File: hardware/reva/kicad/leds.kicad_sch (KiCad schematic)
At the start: 38 parts

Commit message: feat(reva): 15 LED nets on the 595 chain, four more spare outputs
Spec 2026-10-07 section 5: 15 lamps (LED0..LED14), 73 pots. U_SR4 keeps
LED11..LED14 and gains SR_SPARE8..11, marked no-connect (four more test
points would wrap the chains sheet past the A3 title block). BOMs, review
sheet and the leds / mux sheets regenerated with hardware/reva/build.py.

Co-Authored-By: HAL 9000 <293417720+bea-ton-k@users.noreply.github.com>
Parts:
- removed D16: SONG_B_L, LED_THT:LED_D3.0mm, symbol Device:LED
- removed D17: CEIL_L, LED_THT:LED_D3.0mm, symbol Device:LED
- removed D18: CLR_B_L, LED_THT:LED_D3.0mm, symbol Device:LED
- removed D19: MODBTN_L, LED_THT:LED_D3.0mm, symbol Device:LED
- removed R33, R34, R35, R36: 1k, Resistor_SMD:R_0603_1608Metric, symbol Device:R
- D10: value TEMPO_L -> REC_B_L; PanelId TEMPO_L -> REC_B_L
- D11: value REC_B_L -> LVL_B_L; PanelId REC_B_L -> LVL_B_L
- D12: value LVL_B_L -> FTIME_B_L; PanelId LVL_B_L -> FTIME_B_L
- D13: value FLT_B_L -> SONG_B_L; PanelId FLT_B_L -> SONG_B_L
- D14: value SRC_B_L -> GATE_B_L; PanelId SRC_B_L -> GATE_B_L
- D15: value GATE_B_L -> MODBTN_L; PanelId GATE_B_L -> MODBTN_L
- D2: value CLR_A_L -> GATE_A_L; PanelId CLR_A_L -> GATE_A_L
- D4: value GATE_A_L -> FTIME_A_L; PanelId GATE_A_L -> FTIME_A_L
- D5: value SRC_A_L -> LVL_A_L; PanelId SRC_A_L -> LVL_A_L
- D6: value FLT_A_L -> REC_A_L; PanelId FLT_A_L -> REC_A_L
- D7: value REC_A_L -> CLK_L; PanelId REC_A_L -> CLK_L
- D8: value LVL_A_L -> TEMPO_L; PanelId LVL_A_L -> TEMPO_L
- D9: value SYNC_L -> RST_L; PanelId SYNC_L -> RST_L

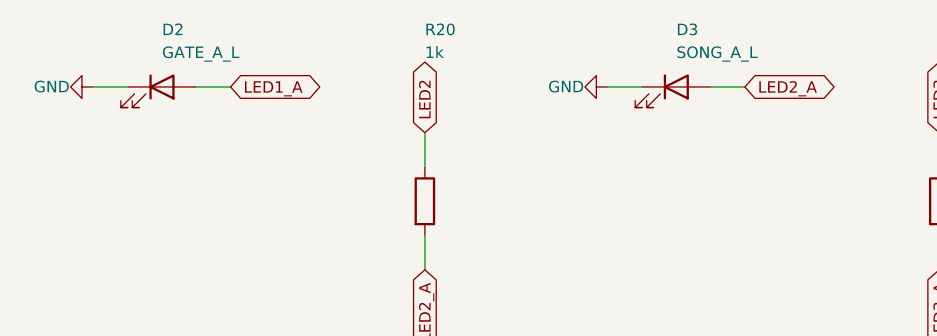
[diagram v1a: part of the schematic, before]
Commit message: chore(reva): panel map and schematic follow the 23.0 centre pitch
assign.py and build.py re-run on the new hole list. The split and the
band counts are unchanged: one split at x = 213.00 (MELODY_B in
SENSE_3's band, the rest of that column in SENSE_1's); bands 20 + 2
calibration / 14 / 15 / 24 pots, 5 spare channels. Inside SENSE_3 nine
centre/deck-B pots change mux channel (the centre columns moved), and
the LED chain swaps SONG_A_L (now index 1) and GATE_A_L (index 2):
SONG's lamp moved down beside its word. Farthest pot from its mux
group's centre: SENSE_2 28.5 -> 27.7 mm, SENSE_3 39.2 -> 36.8 mm.

Co-Authored-By: HAL 9000 <293417720+bea-ton-k@users.noreply.github.com>
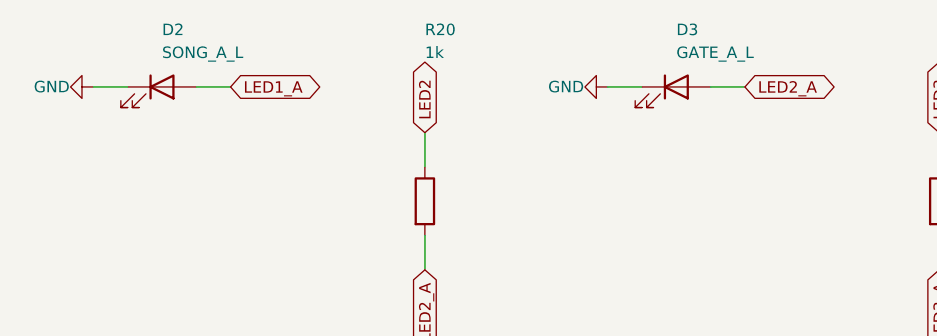
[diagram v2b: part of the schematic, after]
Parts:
- D2: value GATE_A_L -> SONG_A_L; PanelId GATE_A_L -> SONG_A_L
- D3: value SONG_A_L -> GATE_A_L; PanelId SONG_A_L -> GATE_A_L
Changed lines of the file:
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@@
 			(at 107.95 20.32 0)
 			(effects (font (size 1.27 1.27)) (justify left)))
-		(property "Value" "GATE_A_L"
+		(property "Value" "SONG_A_L"
 			(at 107.95 22.86 0)
 			(effects (font (size 1.27 1.27)) (justify left)))
@@
 			(at 107.95 26.67 0)
 			(effects (font (size 1.27 1.27)) (justify left) (hide yes)))
-		(property "PanelId" "GATE_A_L"
+		(property "PanelId" "SONG_A_L"
 			(at 107.95 26.67 0)
 			(effects (font (size 1.27 1.27)) (justify left) (hide yes)))
@@
 			(at 165.1 20.32 0)
 			(effects (font (size 1.27 1.27)) (justify left)))
-		(property "Value" "SONG_A_L"
+		(property "Value" "GATE_A_L"
 			(at 165.1 22.86 0)
 			(effects (font (size 1.27 1.27)) (justify left)))
@@
 			(at 165.1 26.67 0)
 			(effects (font (size 1.27 1.27)) (justify left) (hide yes)))
-		(property "PanelId" "SONG_A_L"
+		(property "PanelId" "GATE_A_L"
 			(at 165.1 26.67 0)
 			(effects (font (size 1.27 1.27)) (justify left) (hide yes)))
